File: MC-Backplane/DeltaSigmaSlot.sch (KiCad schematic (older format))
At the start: 1 part, among them U3 86094328314755V1LF

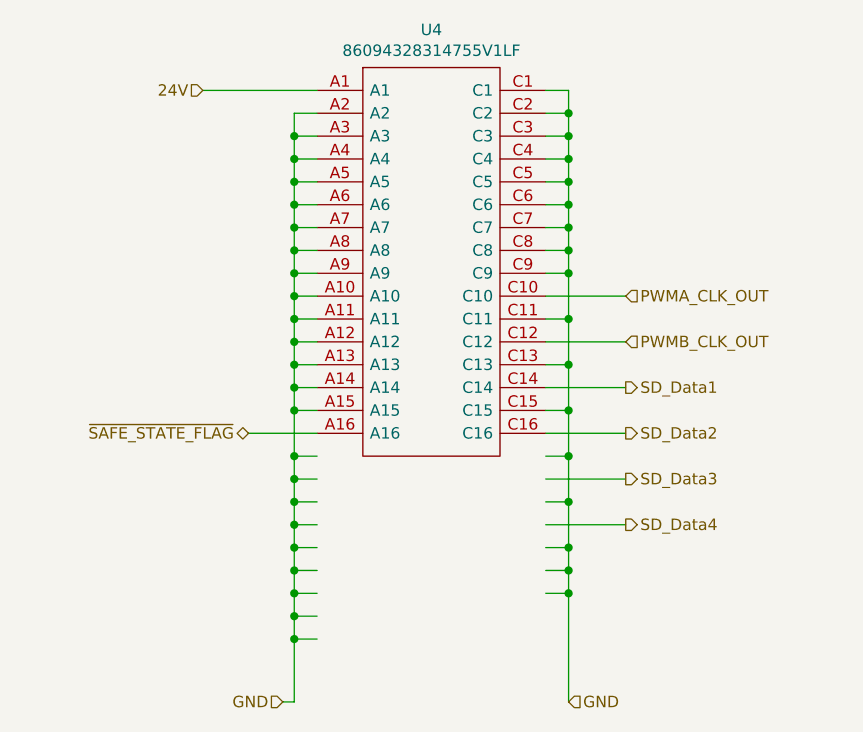
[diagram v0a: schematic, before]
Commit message: placement done- tracks started
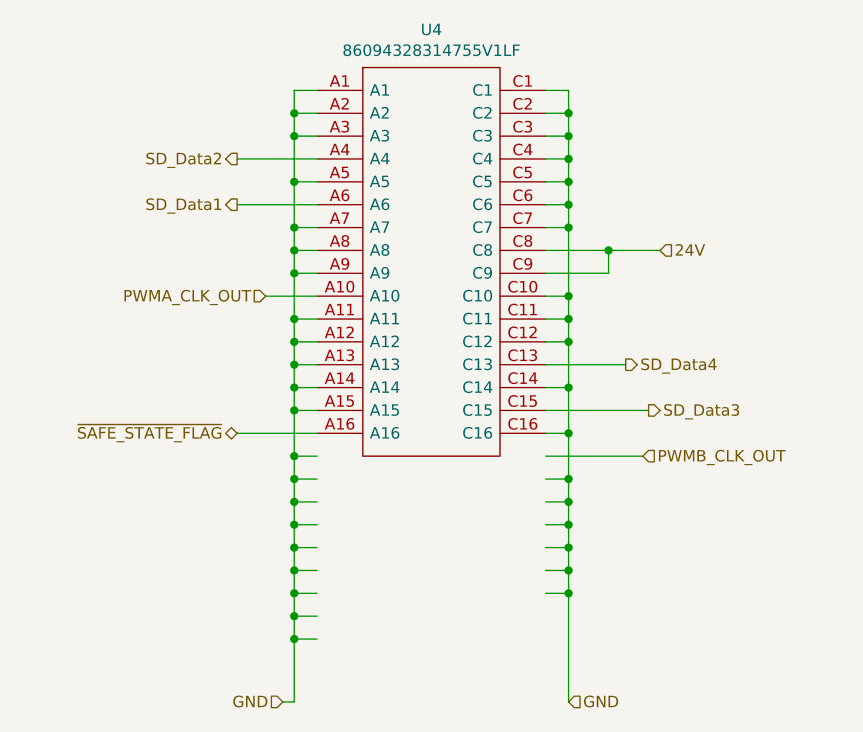
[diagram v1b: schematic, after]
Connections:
- wire segments 89 -> 90
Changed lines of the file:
@@
 Comment4 ""
 $EndDescr
-Text HLabel 6475 3375 2    50   Input ~ 0
-PWMA_CLK_OUT
-Text HLabel 6475 3575 2    50   Input ~ 0
-PWMB_CLK_OUT
 Connection ~ 6225 2975
 Wire Wire Line
@@
 Wire Wire Line
 	6225 2475 6125 2475
-Connection ~ 5025 4075
 Wire Wire Line
 	5125 4075 5025 4075
@@
 Wire Wire Line
 	5025 5150 4975 5150
+Wire Wire Line
+	6225 4675 6225 5150
+Connection ~ 6225 4675
+Wire Wire Line
+	6125 4675 6225 4675
+Text HLabel 4975 5150 0    50   Input ~ 0
+GND
+Text HLabel 6625 3175 2    50   Input ~ 0
+24V
+Text HLabel 6225 5150 2    50   Input ~ 0
+GND
+Wire Wire Line
+	5025 4675 5025 4775
+Wire Wire Line
+	5025 4775 5125 4775
+Wire Wire Line
+	6225 2975 6225 3075
+Wire Wire Line
+	6125 3075 6225 3075
+Connection ~ 5025 4775
+Wire Wire Line
+	5025 4775 5025 4875
+Wire Wire Line
+	6125 4575 6225 4575
+Connection ~ 6225 4575
+Wire Wire Line
+	6225 4575 6225 4675
+Wire Wire Line
+	4775 2975 5125 2975
+Wire Wire Line
+	5125 2875 5025 2875
+Wire Wire Line
+	6475 3675 6125 3675
+Wire Wire Line
+	6125 3775 6225 3775
+Connection ~ 6225 3775
+Wire Wire Line
+	6125 3975 6225 3975
+Connection ~ 6225 3975
+Wire Wire Line
+	5125 3975 4775 3975
+Wire Wire Line
+	6125 3175 6400 3175
+Connection ~ 6225 3075
+Wire Wire Line
+	6125 3275 6400 3275
+Wire Wire Line
+	6400 3275 6400 3175
+Connection ~ 6400 3175
+Wire Wire Line
+	6400 3175 6625 3175
+Wire Wire Line
+	6125 3375 6225 3375
+Wire Wire Line
+	6225 3075 6225 3375
+Connection ~ 6225 3375
+Wire Wire Line
+	5125 3475 5025 3475
+Connection ~ 5025 3475
+Text HLabel 4900 3375 0    50   Input ~ 0
+PWMA_CLK_OUT
+Text HLabel 4775 2975 0    50   Output ~ 0
+SD_Data1
+Text HLabel 6575 3875 2    50   Output ~ 0
+SD_Data3
+Text HLabel 4775 3975 0    50   BiDi ~ 0
+~SAFE_STATE_FLAG~
+Wire Wire Line
+	6125 3875 6575 3875
+Wire Wire Line
+	6125 4075 6550 4075
+Text HLabel 6550 4075 2    50   Input ~ 0
+PWMB_CLK_OUT
+Wire Wire Line
+	6125 4175 6225 4175
+Connection ~ 6225 4175
+Wire Wire Line
+	6225 4175 6225 4275
+Wire Wire Line
+	6125 4375 6225 4375
+Connection ~ 6225 4375
+Wire Wire Line
+	6225 4375 6225 4475
+Wire Wire Line
+	6225 3375 6225 3475
+Wire Wire Line
+	6225 3775 6225 3975
+Wire Wire Line
+	6125 3575 6225 3575
+Connection ~ 6225 3575
+Wire Wire Line
+	5125 3675 5025 3675
+Wire Wire Line
+	5125 3775 5025 3775
+Wire Wire Line
+	5025 3775 5025 3675
+Connection ~ 5025 3675
+Wire Wire Line
+	5125 3875 5025 3875
+Wire Wire Line
+	5025 3875 5025 3775
+Connection ~ 5025 3775
+Wire Wire Line
+	5125 3575 5025 3575
+Wire Wire Line
+	5025 3475 5025 3575
+Connection ~ 5025 3575
+Wire Wire Line
+	5025 3575 5025 3675
+Connection ~ 5025 2875
+Wire Wire Line
+	5125 3375 4900 3375
+Wire Wire Line
+	5025 2875 5025 3075
+Text HLabel 4775 2775 0    50   Output ~ 0
+SD_Data2
+Text HLabel 6475 3675 2    50   Output ~ 0
+SD_Data4
+Wire Wire Line
+	5125 2675 5025 2675
 $Comp
 L Existing_IC_Models:86094328314755V1LF U?
@@
 $EndComp
 Wire Wire Line
-	5125 3875 5025 3875
-Wire Wire Line
-	6225 4675 6225 5150
-Connection ~ 6225 4675
-Wire Wire Line
-	6125 4675 6225 4675
-Text HLabel 4825 3975 0    50   BiDi ~ 0
-~SAFE_STATE_FLAG~
-Text HLabel 6475 3975 2    50   Output ~ 0
-SD_Data2
-Text HLabel 6475 3775 2    50   Output ~ 0
-SD_Data1
-Wire Wire Line
-	6225 3275 6225 3175
-Connection ~ 6225 3275
-Wire Wire Line
-	6125 3275 6225 3275
+	4775 2775 5125 2775
+Wire Wire Line
+	5025 2675 5025 2575
+Wire Wire Line
+	5025 2475 5125 2475
+Connection ~ 5025 2675
+Wire Wire Line
+	5125 3075 5025 3075
+Connection ~ 5025 3075
+Wire Wire Line
+	5025 3075 5025 3175
+Wire Wire Line
+	5125 3275 5025 3275
+Connection ~ 5025 3275
+Wire Wire Line
+	6225 3975 6225 4175
+Connection ~ 6225 3475
+Wire Wire Line
+	6225 3475 6225 3575
+Wire Wire Line
+	6125 3475 6225 3475
+Wire Wire Line
+	5025 3875 5025 4075
+Connection ~ 5025 3875
+Connection ~ 5025 4075
 Connection ~ 6225 4275
 Wire Wire Line
+	6225 4275 6225 4375
+Wire Wire Line
 	6125 4275 6225 4275
 Wire Wire Line
-	6225 4075 6225 4275
-Connection ~ 6225 4075
-Wire Wire Line
-	6125 4075 6225 4075
-Wire Wire Line
-	6225 3875 6225 4075
-Connection ~ 6225 3875
-Wire Wire Line
-	6125 3875 6225 3875
-Wire Wire Line
-	6225 3675 6225 3875
-Connection ~ 6225 3675
-Wire Wire Line
-	6125 3675 6225 3675
-Wire Wire Line
-	6225 3475 6225 3675
-Connection ~ 6225 3475
-Wire Wire Line
-	6125 3475 6225 3475
-Wire Wire Line
-	6225 4275 6225 4475
+	6125 4475 6225 4475
 Connection ~ 6225 4475
 Wire Wire Line
-	6125 4475 6225 4475
-Wire Wire Line
-	5025 3775 5025 3875
-Connection ~ 5025 3775
-Wire Wire Line
-	5125 3775 5025 3775
-Wire Wire Line
-	5025 3575 5025 3675
-Connection ~ 5025 3575
-Wire Wire Line
-	5125 3575 5025 3575
-Wire Wire Line
-	5025 3375 5025 3475
-Connection ~ 5025 3375
-Wire Wire Line
-	5125 3375 5025 3375
+	6225 4475 6225 4575
+Wire Wire Line
+	6225 3575 6225 3775
+Wire Wire Line
+	5125 2575 5025 2575
+Wire Wire Line
+	5025 3275 5025 3475
+Wire Wire Line
+	5125 3175 5025 3175
+Connection ~ 5025 3175
 Wire Wire Line
 	5025 3175 5025 3275
-Connection ~ 5025 3175
-Wire Wire Line
-	5125 3175 5025 3175
-Wire Wire Line
-	5025 2975 5025 3075
-Connection ~ 5025 2975
-Wire Wire Line
-	5125 2975 5025 2975
-Wire Wire Line
-	5025 2675 5025 2775
-Wire Wire Line
-	5025 2775 5025 2875
-Connection ~ 5025 2775
-Wire Wire Line
-	5125 2775 5025 2775
-Wire Wire Line
-	5125 2675 5025 2675
-Connection ~ 5025 2675
-Wire Wire Line
-	5025 2575 5025 2675
-Wire Wire Line
-	5125 2575 5025 2575
-Text HLabel 4975 5150 0    50   Input ~ 0
-GND
-Wire Wire Line
-	6475 4375 6125 4375
-Wire Wire Line
-	6125 4175 6475 4175
-Wire Wire Line
-	6475 3975 6125 3975
-Wire Wire Line
-	6125 3575 6475 3575
-Wire Wire Line
-	5125 3675 5025 3675
-Wire Wire Line
-	5125 3475 5025 3475
-Wire Wire Line
-	5125 3275 5025 3275
-Wire Wire Line
-	5125 3075 5025 3075
-Wire Wire Line
-	5125 2875 5025 2875
-Wire Wire Line
-	5125 2475 4625 2475
-Text HLabel 4625 2475 0    50   Input ~ 0
-24V
-Text HLabel 6225 5150 2    50   Input ~ 0
-GND
-Wire Wire Line
-	6125 3175 6225 3175
-Connection ~ 6225 3175
-Wire Wire Line
-	5025 4675 5025 4775
-Wire Wire Line
-	5025 4775 5125 4775
-Connection ~ 5025 3875
-Connection ~ 5025 2875
-Wire Wire Line
-	5025 2875 5025 2975
-Connection ~ 5025 3075
-Wire Wire Line
-	5025 3075 5025 3175
-Connection ~ 5025 3275
-Wire Wire Line
-	5025 3275 5025 3375
-Connection ~ 5025 3475
-Wire Wire Line
-	5025 3475 5025 3575
-Connection ~ 5025 3675
-Wire Wire Line
-	5025 3675 5025 3775
-Wire Wire Line
-	6225 2975 6225 3075
-Wire Wire Line
-	6125 3075 6225 3075
-Connection ~ 6225 3075
-Wire Wire Line
-	6225 3075 6225 3175
-Wire Wire Line
-	6225 3275 6225 3475
-Wire Wire Line
-	6475 3375 6125 3375
-Wire Wire Line
-	5025 3875 5025 4075
-Connection ~ 5025 4775
-Wire Wire Line
-	5025 4775 5025 4875
-Wire Wire Line
-	5125 3975 4825 3975
-Wire Wire Line
-	6225 4475 6225 4575
-Wire Wire Line
-	6125 4575 6225 4575
-Connection ~ 6225 4575
-Wire Wire Line
-	6225 4575 6225 4675
-Text HLabel 6475 4375 2    50   Output ~ 0
-SD_Data4
-Text HLabel 6475 4175 2    50   Output ~ 0
-SD_Data3
-Wire Wire Line
-	6125 3775 6475 3775
+Connection ~ 5025 2575
+Wire Wire Line
+	5025 2575 5025 2475
+Wire Wire Line
+	5025 2675 5025 2875
 $EndSCHEMATC

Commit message: layout done: cleaning up and checking MH
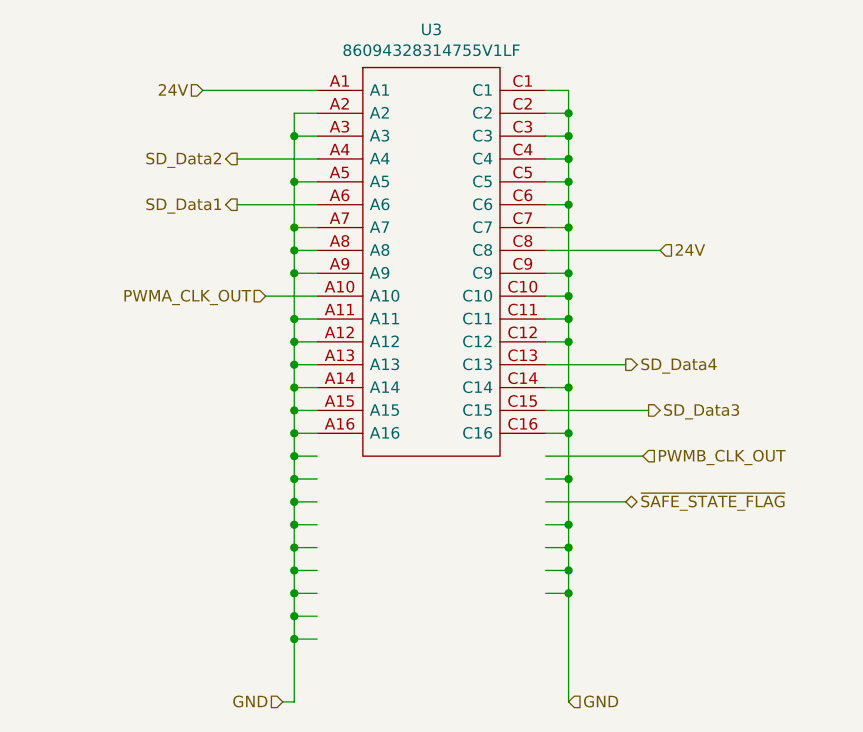
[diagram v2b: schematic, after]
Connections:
- wire segments 90 -> 88
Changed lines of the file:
@@
 $Descr A4 11693 8268
 encoding utf-8
-Sheet 4 14
+Sheet 3 14
 Title ""
 Date ""
@@
 Connection ~ 6225 3975
 Wire Wire Line
-	5125 3975 4775 3975
-Wire Wire Line
-	6125 3175 6400 3175
+	6125 4275 6475 4275
 Connection ~ 6225 3075
 Wire Wire Line
-	6125 3275 6400 3275
-Wire Wire Line
-	6400 3275 6400 3175
-Connection ~ 6400 3175
-Wire Wire Line
-	6400 3175 6625 3175
-Wire Wire Line
 	6125 3375 6225 3375
 Wire Wire Line
-	6225 3075 6225 3375
+	6225 3075 6225 3275
 Connection ~ 6225 3375
 Wire Wire Line
@@
 Text HLabel 6575 3875 2    50   Output ~ 0
 SD_Data3
-Text HLabel 4775 3975 0    50   BiDi ~ 0
+Text HLabel 6475 4275 2    50   BiDi ~ 0
 ~SAFE_STATE_FLAG~
 Wire Wire Line
@@
 	6125 4175 6225 4175
 Connection ~ 6225 4175
-Wire Wire Line
-	6225 4175 6225 4275
 Wire Wire Line
 	6125 4375 6225 4375
@@
 AR Path="/6231C7B7/622C3C12" Ref="U3"  Part="1"
 AR Path="/6234E41C/622C3C12" Ref="U4"  Part="1"
-F 0 "U4" H 5625 2740 50  0000 C CNN
+F 0 "U3" H 5625 2740 50  0000 C CNN
 F 1 "86094328314755V1LF" H 5625 2649 50  0000 C CNN
 F 2 "Footprints_MC-Backplane:86094328314755V1LF" V 5975 2575 50  0001 L CNN
@@
 Wire Wire Line
 	5025 2675 5025 2575
-Wire Wire Line
-	5025 2475 5125 2475
 Connection ~ 5025 2675
 Wire Wire Line
@@
 	6125 3475 6225 3475
 Wire Wire Line
-	5025 3875 5025 4075
+	5025 3875 5025 3975
 Connection ~ 5025 3875
 Connection ~ 5025 4075
-Connection ~ 6225 4275
-Wire Wire Line
-	6225 4275 6225 4375
-Wire Wire Line
-	6125 4275 6225 4275
 Wire Wire Line
 	6125 4475 6225 4475
@@
 Wire Wire Line
 	5025 3175 5025 3275
-Connection ~ 5025 2575
-Wire Wire Line
-	5025 2575 5025 2475
 Wire Wire Line
 	5025 2675 5025 2875
+Wire Wire Line
+	6225 4175 6225 4375
+Wire Wire Line
+	5125 3975 5025 3975
+Connection ~ 5025 3975
+Wire Wire Line
+	5025 3975 5025 4075
+Wire Wire Line
+	6125 3175 6625 3175
+Wire Wire Line
+	6125 3275 6225 3275
+Connection ~ 6225 3275
+Wire Wire Line
+	6225 3275 6225 3375
+Text HLabel 4625 2475 0    50   Input ~ 0
+24V
+Wire Wire Line
+	4625 2475 5125 2475
 $EndSCHEMATC

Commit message: Layout ready for review
- double check measurements and connector placement
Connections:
- wire segments 88 -> 56
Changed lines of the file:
@@
 Comment4 ""
 $EndDescr
-Connection ~ 6225 2975
 Wire Wire Line
-	6125 2975 6225 2975
+	5025 4450 4925 4450
 Wire Wire Line
-	6225 2975 6225 2875
-Connection ~ 6225 2875
+	6225 3975 6225 4450
+Connection ~ 6225 3975
 Wire Wire Line
-	6125 2875 6225 2875
-Wire Wire Line
-	6225 2875 6225 2775
-Connection ~ 6225 2775
-Wire Wire Line
-	6225 2775 6125 2775
-Wire Wire Line
-	6225 2775 6225 2675
-Connection ~ 6225 2675
-Wire Wire Line
-	6125 2675 6225 2675
-Wire Wire Line
-	6225 2675 6225 2575
-Wire Wire Line
-	6225 2575 6225 2475
-Connection ~ 6225 2575
-Wire Wire Line
-	6125 2575 6225 2575
-Wire Wire Line
-	6225 2475 6125 2475
-Wire Wire Line
-	5125 4075 5025 4075
-Wire Wire Line
-	5025 4075 5025 4175
-Connection ~ 5025 4175
-Wire Wire Line
-	5025 4175 5125 4175
-Wire Wire Line
-	5025 4175 5025 4275
-Connection ~ 5025 4275
-Wire Wire Line
-	5025 4275 5125 4275
-Wire Wire Line
-	5025 4275 5025 4375
-Connection ~ 5025 4375
-Wire Wire Line
-	5125 4375 5025 4375
-Wire Wire Line
-	5025 4375 5025 4475
-Connection ~ 5025 4475
-Wire Wire Line
-	5125 4475 5025 4475
-Wire Wire Line
-	5025 4475 5025 4575
-Connection ~ 5025 4575
-Wire Wire Line
-	5125 4575 5025 4575
-Wire Wire Line
-	5025 4575 5025 4675
-Connection ~ 5025 4675
-Wire Wire Line
-	5125 4675 5025 4675
-Wire Wire Line
-	5125 4875 5025 4875
-Wire Wire Line
-	5025 4875 5025 5150
-Connection ~ 5025 4875
-Wire Wire Line
-	5025 5150 4975 5150
-Wire Wire Line
-	6225 4675 6225 5150
-Connection ~ 6225 4675
-Wire Wire Line
-	6125 4675 6225 4675
-Text HLabel 4975 5150 0    50   Input ~ 0
+	6125 3975 6225 3975
+Text HLabel 4925 4450 0    50   Input ~ 0
 GND
-Text HLabel 6625 3175 2    50   Input ~ 0
+Text HLabel 6625 2475 2    50   Input ~ 0
 24V
-Text HLabel 6225 5150 2    50   Input ~ 0
+Text HLabel 6225 4450 2    50   Input ~ 0
 GND
 Wire Wire Line
-	5025 4675 5025 4775
+	6125 3875 6225 3875
+Connection ~ 6225 3875
 Wire Wire Line
-	5025 4775 5125 4775
-Wire Wire Line
-	6225 2975 6225 3075
-Wire Wire Line
-	6125 3075 6225 3075
-Connection ~ 5025 4775
-Wire Wire Line
-	5025 4775 5025 4875
-Wire Wire Line
-	6125 4575 6225 4575
-Connection ~ 6225 4575
-Wire Wire Line
-	6225 4575 6225 4675
+	6225 3875 6225 3975
 Wire Wire Line
 	4775 2975 5125 2975
@@
 	5125 2875 5025 2875
 Wire Wire Line
-	6475 3675 6125 3675
+	6475 2975 6125 2975
 Wire Wire Line
-	6125 3775 6225 3775
-Connection ~ 6225 3775
-Wire Wire Line
-	6125 3975 6225 3975
-Connection ~ 6225 3975
-Wire Wire Line
-	6125 4275 6475 4275
+	6125 3075 6225 3075
 Connection ~ 6225 3075
 Wire Wire Line
-	6125 3375 6225 3375
+	6125 3275 6225 3275
+Connection ~ 6225 3275
 Wire Wire Line
-	6225 3075 6225 3275
-Connection ~ 6225 3375
+	6125 3575 6475 3575
+Wire Wire Line
+	6125 2675 6225 2675
+Connection ~ 6225 2675
 Wire Wire Line
 	5125 3475 5025 3475
@@
 Text HLabel 4775 2975 0    50   Output ~ 0
 SD_Data1
-Text HLabel 6575 3875 2    50   Output ~ 0
+Text HLabel 6575 3175 2    50   Output ~ 0
 SD_Data3
-Text HLabel 6475 4275 2    50   BiDi ~ 0
+Text HLabel 6475 3575 2    50   BiDi ~ 0
 ~SAFE_STATE_FLAG~
 Wire Wire Line
-	6125 3875 6575 3875
+	6125 3175 6575 3175
 Wire Wire Line
-	6125 4075 6550 4075
-Text HLabel 6550 4075 2    50   Input ~ 0
+	6125 3375 6550 3375
+Text HLabel 6550 3375 2    50   Input ~ 0
 PWMB_CLK_OUT
 Wire Wire Line
-	6125 4175 6225 4175
-Connection ~ 6225 4175
+	6125 3475 6225 3475
+Connection ~ 6225 3475
 Wire Wire Line
-	6125 4375 6225 4375
-Connection ~ 6225 4375
+	6125 3675 6225 3675
+Connection ~ 6225 3675
 Wire Wire Line
-	6225 4375 6225 4475
+	6225 3675 6225 3775
 Wire Wire Line
-	6225 3375 6225 3475
+	6225 2675 6225 2775
 Wire Wire Line
-	6225 3775 6225 3975
+	6225 3075 6225 3275
 Wire Wire Line
-	6125 3575 6225 3575
-Connection ~ 6225 3575
+	6125 2875 6225 2875
+Connection ~ 6225 2875
 Wire Wire Line
 	5125 3675 5025 3675
@@
 Text HLabel 4775 2775 0    50   Output ~ 0
 SD_Data2
-Text HLabel 6475 3675 2    50   Output ~ 0
+Text HLabel 6475 2975 2    50   Output ~ 0
 SD_Data4
 Wire Wire Line
@@
 Connection ~ 5025 3275
 Wire Wire Line
-	6225 3975 6225 4175
-Connection ~ 6225 3475
+	6225 3275 6225 3475
+Connection ~ 6225 2775
 Wire Wire Line
-	6225 3475 6225 3575
+	6225 2775 6225 2875
 Wire Wire Line
-	6125 3475 6225 3475
+	6125 2775 6225 2775
 Wire Wire Line
 	5025 3875 5025 3975
 Connection ~ 5025 3875
-Connection ~ 5025 4075
 Wire Wire Line
-	6125 4475 6225 4475
-Connection ~ 6225 4475
+	6125 3775 6225 3775
+Connection ~ 6225 3775
 Wire Wire Line
-	6225 4475 6225 4575
+	6225 3775 6225 3875
 Wire Wire Line
-	6225 3575 6225 3775
+	6225 2875 6225 3075
 Wire Wire Line
 	5125 2575 5025 2575
@@
 	5025 2675 5025 2875
 Wire Wire Line
-	6225 4175 6225 4375
+	6225 3475 6225 3675
 Wire Wire Line
 	5125 3975 5025 3975
-Connection ~ 5025 3975
 Wire Wire Line
-	5025 3975 5025 4075
+	6125 2475 6625 2475
 Wire Wire Line
-	6125 3175 6625 3175
+	6125 2575 6225 2575
 Wire Wire Line
-	6125 3275 6225 3275
-Connection ~ 6225 3275
-Wire Wire Line
-	6225 3275 6225 3375
+	6225 2575 6225 2675
 Text HLabel 4625 2475 0    50   Input ~ 0
 24V
 Wire Wire Line
 	4625 2475 5125 2475
+Wire Wire Line
+	5025 3975 5025 4450
+Connection ~ 5025 3975
 $EndSCHEMATC

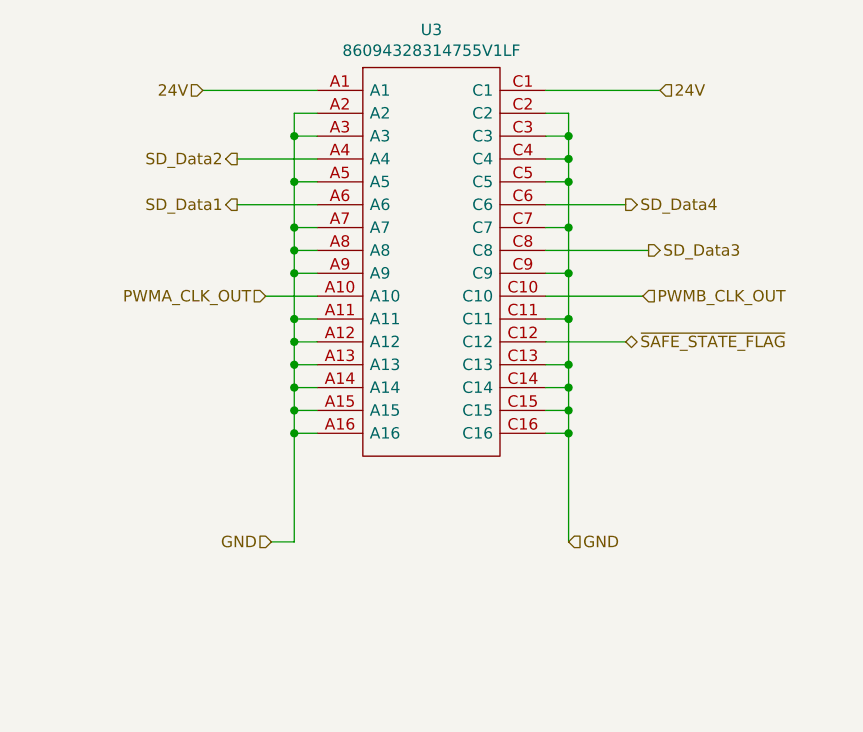
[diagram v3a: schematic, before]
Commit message: spread tracks across available space
could still add some test points
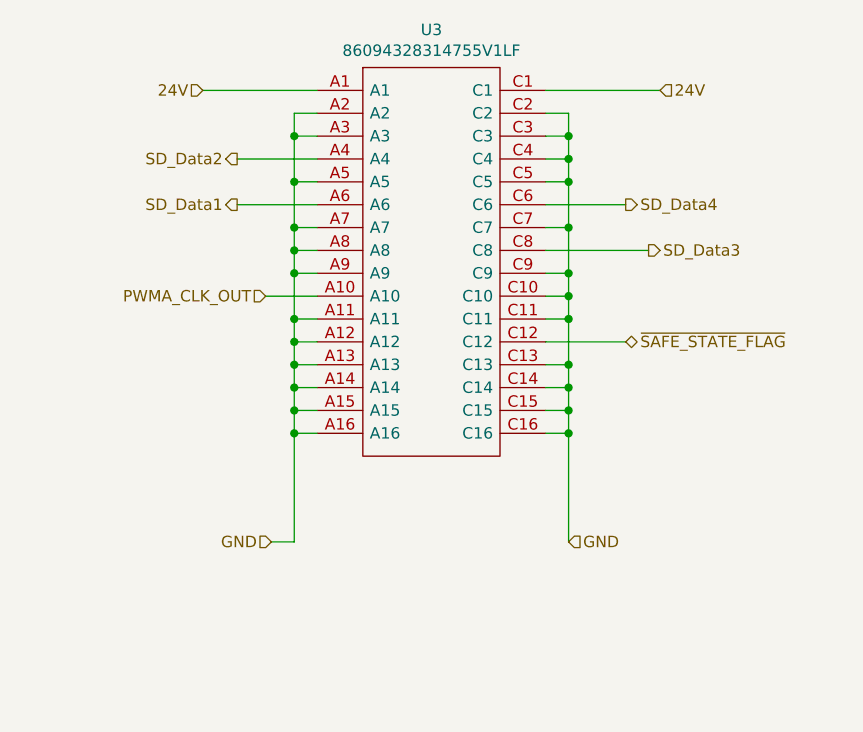
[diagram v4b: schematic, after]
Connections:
- net PWMB_CLK_OUT is gone; now on net GND: U3.C10
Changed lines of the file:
@@
 	6125 3175 6575 3175
 Wire Wire Line
-	6125 3375 6550 3375
-Text HLabel 6550 3375 2    50   Input ~ 0
-PWMB_CLK_OUT
+	6125 3375 6225 3375
 Wire Wire Line
 	6125 3475 6225 3475
@@
 Connection ~ 5025 3275
 Wire Wire Line
-	6225 3275 6225 3475
+	6225 3275 6225 3375
 Connection ~ 6225 2775
 Wire Wire Line
@@
 	5025 3975 5025 4450
 Connection ~ 5025 3975
+Connection ~ 6225 3375
+Wire Wire Line
+	6225 3375 6225 3475
 $EndSCHEMATC
